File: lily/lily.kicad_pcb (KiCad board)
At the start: 4 copper layers, 70.7 x 53.3 mm, 23 parts, among them J1 NEIGHBOR1, J10 TEST_2P, J2 NEIGHBOR2, J3 ANT_IN, J4 TEST_2P, J5 TEST_2P, J6 TEST_2P, J7 BONUS_ROW, J8 TEST_2P, J9 TEST_2P, U1 ADL5904

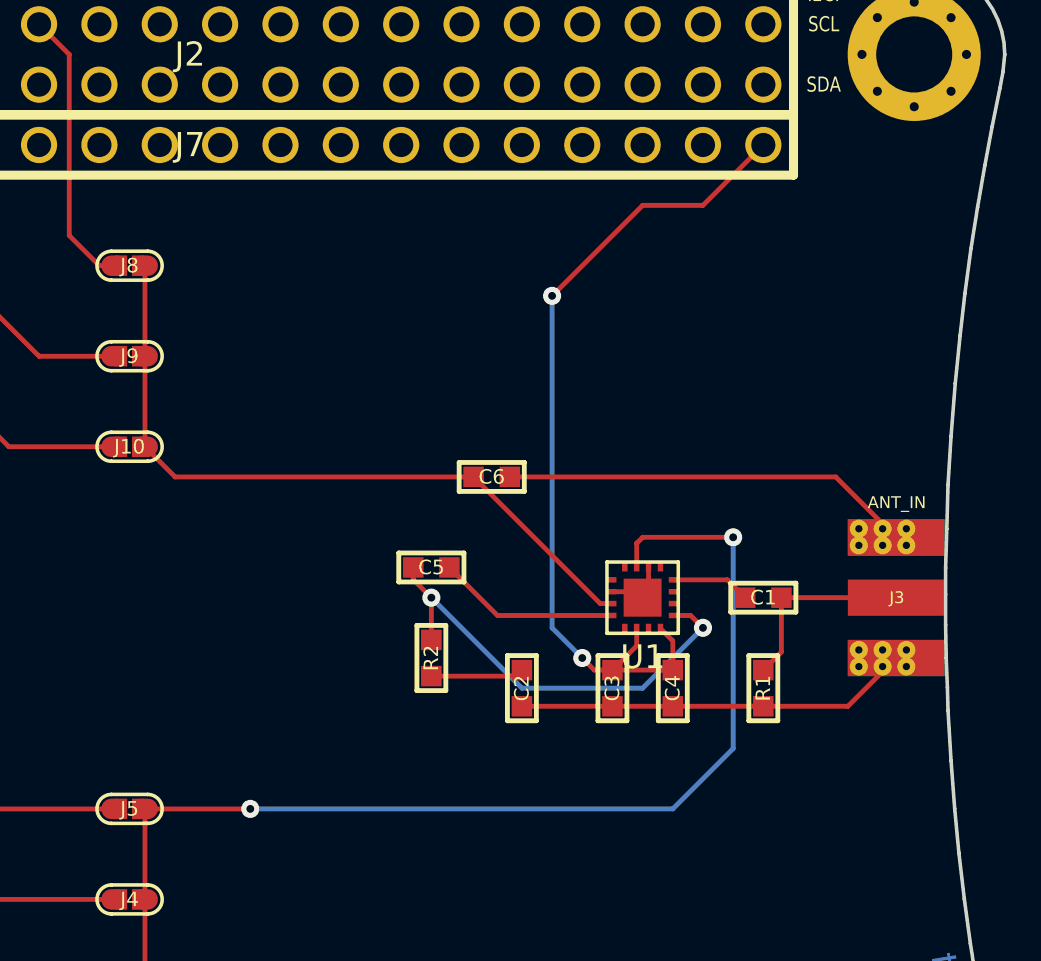
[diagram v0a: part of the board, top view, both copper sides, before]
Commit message: Updated copper pours on Lily PCB layout, added comments on schematic.
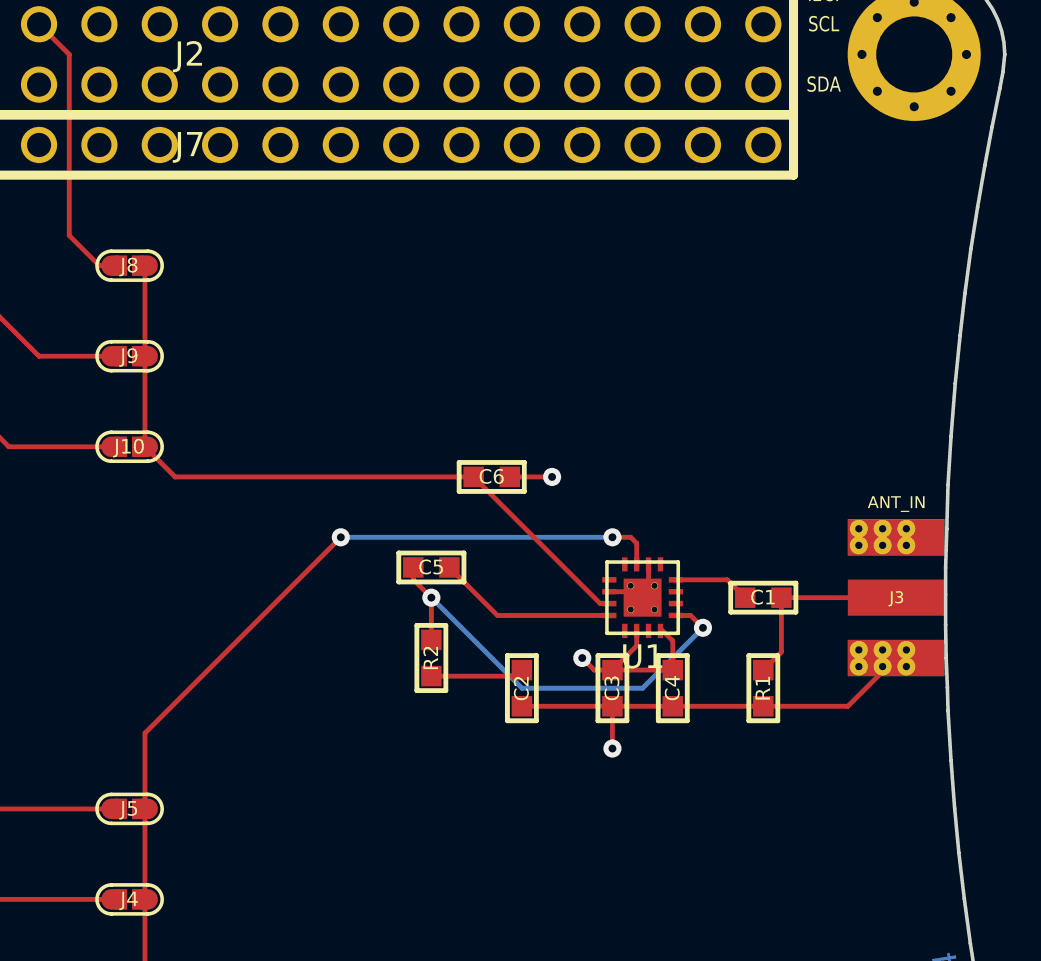
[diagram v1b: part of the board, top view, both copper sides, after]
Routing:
- net VCC: track 35.4 -> 8.15 mm, vias 2 -> 1
- net GND: track 36.7 -> 23.0 mm, vias 0 -> 2
- net /ENBL: track 47.5 -> 36.0 mm

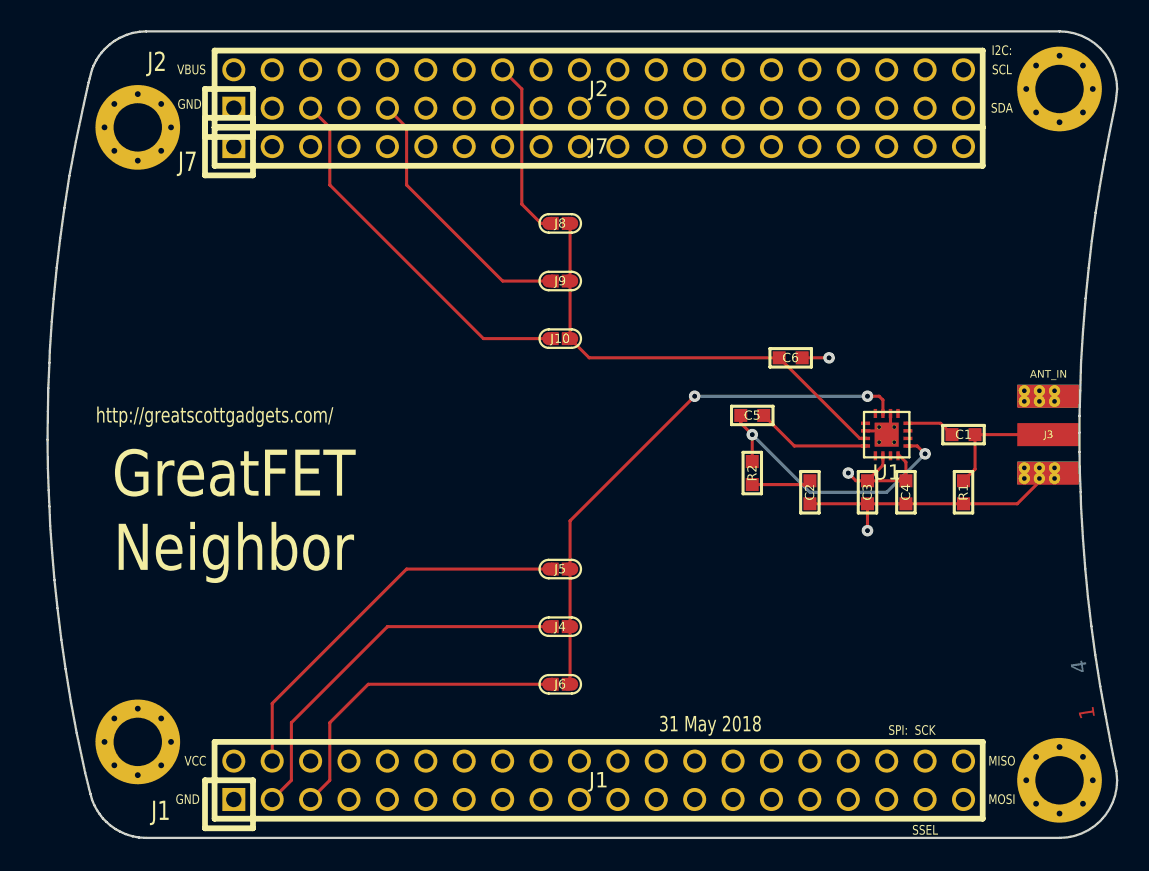
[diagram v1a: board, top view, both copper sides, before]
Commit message: Revised Lily schematic and PCB: Added connections for threshold detection mode and improved RF impedance matching.
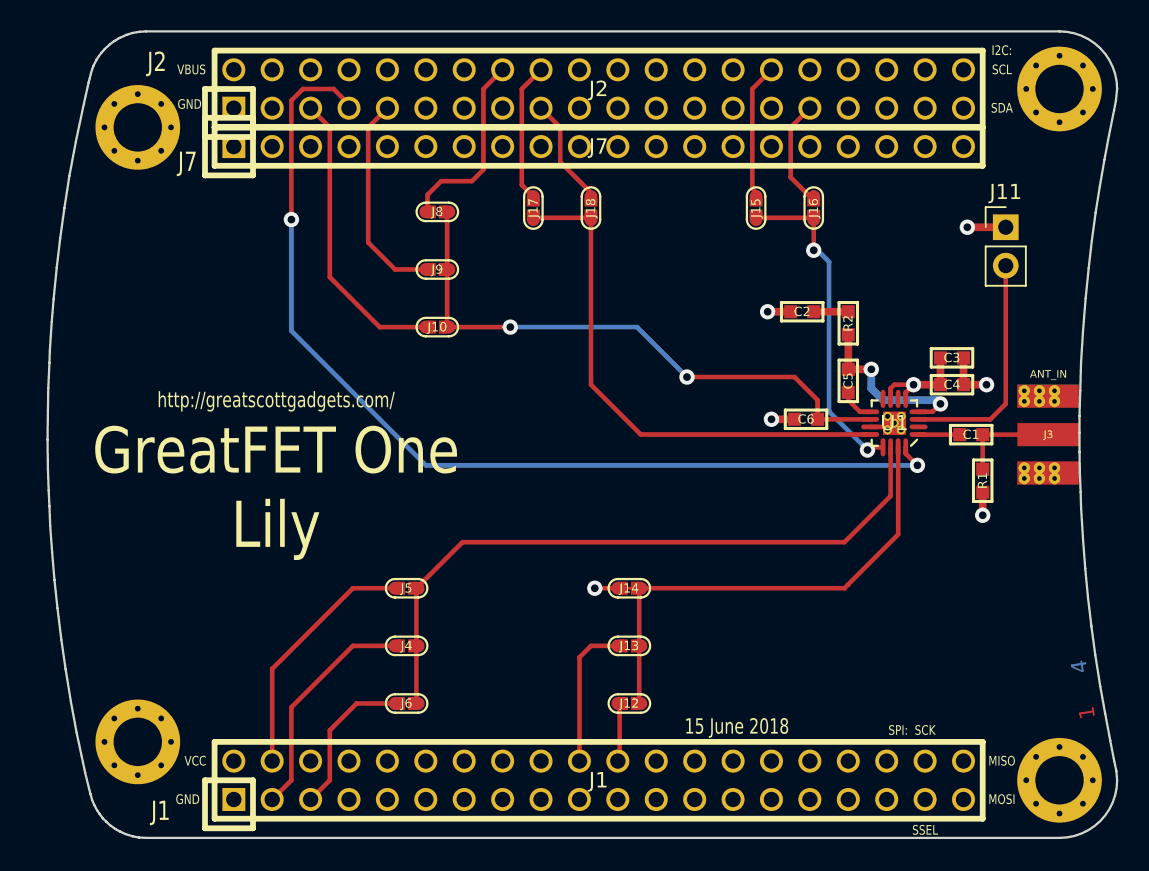
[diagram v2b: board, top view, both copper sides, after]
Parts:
- added J11: Conn_01x02, Pin_Headers:Pin_Header_Straight_1x02_Pitch2.54mm, F.Cu at (173.0, 81.5)
- added J12: TEST_2P, gsg-modules:0603-JUMPER, F.Cu at (148.1, 113.0)
- added J13: TEST_2P, gsg-modules:0603-JUMPER, F.Cu at (148.1, 109.2)
- added J14: TEST_2P, gsg-modules:0603-JUMPER, F.Cu at (148.1, 105.4)
- added J15: TEST_2P, gsg-modules:0603-JUMPER, F.Cu at (156.5, 80.3)
- added J16: TEST_2P, gsg-modules:0603-JUMPER, F.Cu at (160.3, 80.3)
- added J17: TEST_2P, gsg-modules:0603-JUMPER, F.Cu at (141.7, 80.3)
- added J18: TEST_2P, gsg-modules:0603-JUMPER, F.Cu at (145.5, 80.3)
- C3: value 0.1uF -> 100nF
- C5: value Crms -> 100nF
- U1: footprint gsg-modules:ADL5904 -> gsg-modules:QFN16-3
- moved C2 11.9 mm to (159.5, 87.1), turned to 180 degrees
- moved R2 11.8 mm to (162.6, 87.9), turned to 90 degrees
- moved C3 10.5 mm to (169.4, 90.2), turned to 0 degrees
- moved J4 10.2 mm to (133.3, 109.2)
- moved J5 10.2 mm to (133.3, 105.4)
- moved J6 10.2 mm to (133.3, 113.0)
- moved J10 8.16 mm to (135.4, 88.1)
- moved J8 8.16 mm to (135.4, 80.5)
- moved J9 8.16 mm to (135.4, 84.3)
- moved C4 7.74 mm to (169.4, 91.9), turned to 0 degrees
- moved C5 6.75 mm to (162.6, 91.7), turned to 90 degrees
- moved C6 4.19 mm to (159.8, 94.2), turned to 180 degrees
- moved R1 1.48 mm to (171.4, 98.3)
- moved U1 0.92 mm to (165.6, 94.5), turned to 180 degrees
- moved C1 0.51 mm to (170.7, 95.2)
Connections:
- net Net-(J2-Pad2) renamed /VBUS
- U1 pad 15: GND -> Net-(J12-Pad2)
- U1 pad 16: Net-(U1-Pad16) -> /P4_4
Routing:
- net /P4_4: track 0.00 -> 66.6 mm, vias 0 -> 2
- net Net-(J17-Pad1): track 0.00 -> 34.7 mm
- net Net-(J12-Pad2): track 0.00 -> 32.0 mm
- net Net-(J15-Pad1): track 0.00 -> 21.9 mm, vias 0 -> 2
- net Net-(J11-Pad2): track 0.00 -> 15.3 mm
- net /P4_10: track 21.3 -> 10.3 mm
- net /P4_9: track 25.4 -> 15.3 mm
- net /P1_10: track 0.00 -> 9.83 mm
- net /P2_5: track 0.00 -> 9.34 mm
- net /P3_7: track 0.00 -> 9.13 mm
- net /P0_0: track 25.9 -> 16.8 mm
- net /VOUT: track 30.0 -> 38.9 mm, vias 0 -> 2
- net /ENBL: track 36.0 -> 44.7 mm, vias 2 -> 0
- net GND: track 23.0 -> 14.8 mm, vias 2 -> 6
- net /WAKEUP0: track 0.00 -> 7.32 mm
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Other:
- board text added: "15 June 2018"
- board text added: "GreatFET One Lily"
- board text removed: "31 May 2018"
- board text removed: "GreatFET Neighbor"
- board text removed: "need to connect exposed pad to ground plane"

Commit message: Revised Lily PCB: added silkscreen labels, rerouted tracks, etc.
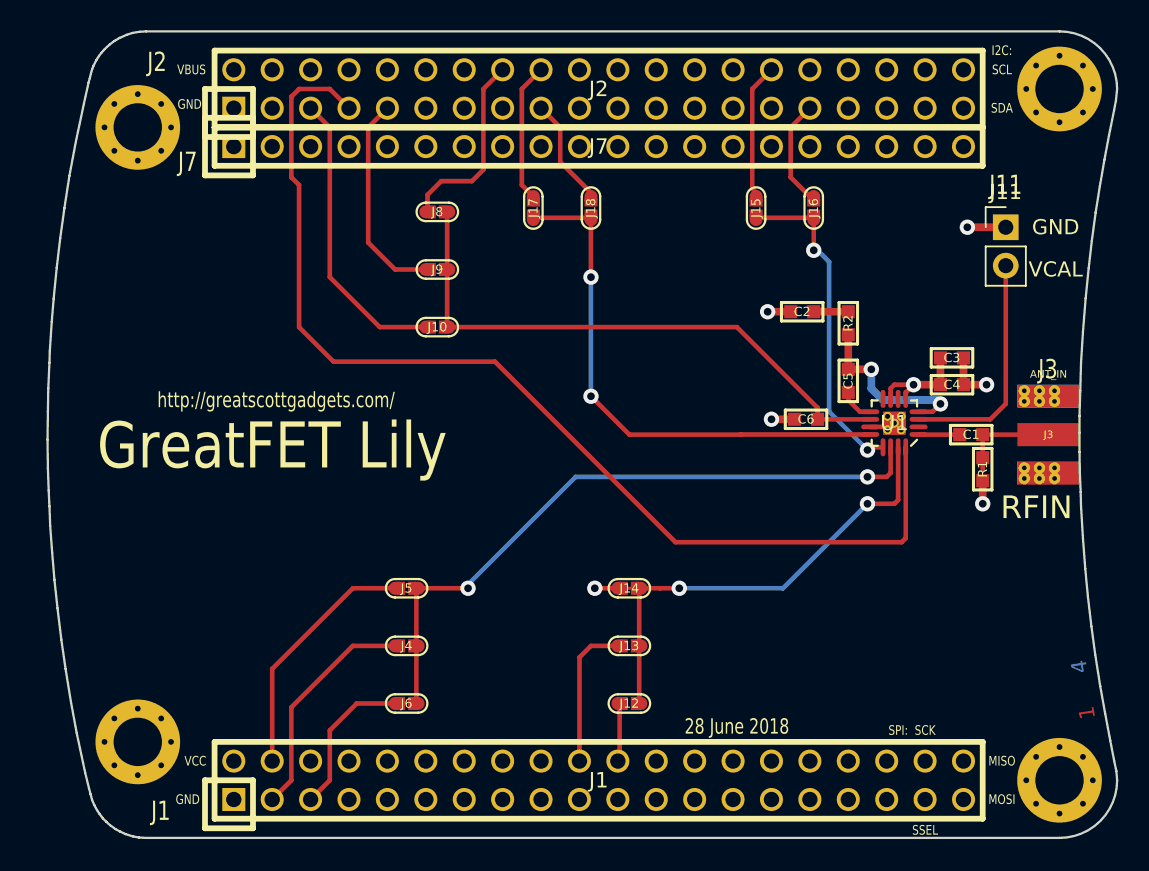
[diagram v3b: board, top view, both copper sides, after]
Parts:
- moved R1 0.76 mm to (171.4, 97.5)
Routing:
- net /P4_4: track 66.6 -> 72.8 mm, vias 2 -> 0
- net Net-(J12-Pad2): track 32.0 -> 30.7 mm, vias 0 -> 2
- net /ENBL: track 44.7 -> 44.0 mm, vias 0 -> 2
- net Net-(J17-Pad1): track 34.7 -> 35.1 mm, vias 0 -> 2
- net /VOUT: track 38.9 -> 38.6 mm, vias 2 -> 0
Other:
- board text added: "28 June 2018"
- board text added: "GreatFET Lily"
- board text added: "J11"
- board text added: "J3"
- board text added: "RFIN"
- board text added: "VCAL"
- board text removed: "15 June 2018"
- board text removed: "GreatFET One Lily"

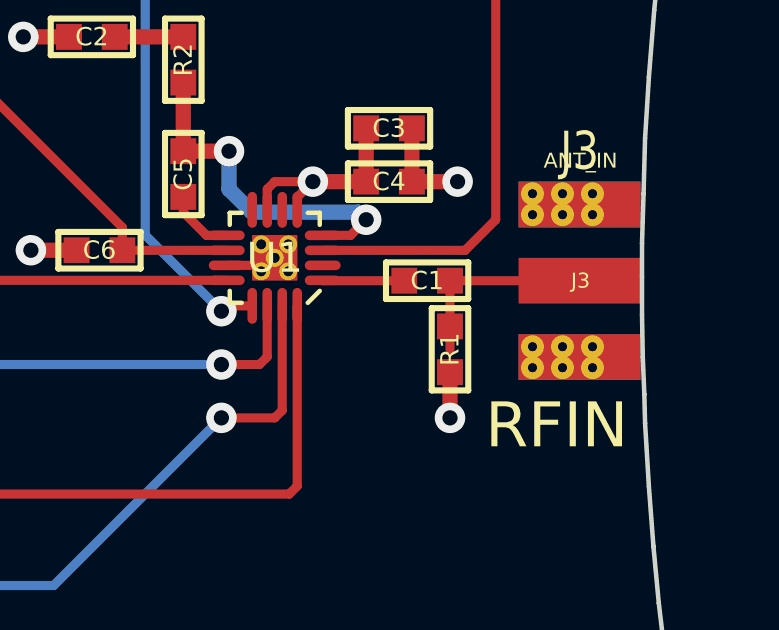
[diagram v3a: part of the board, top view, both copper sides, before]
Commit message: Fixed bad track
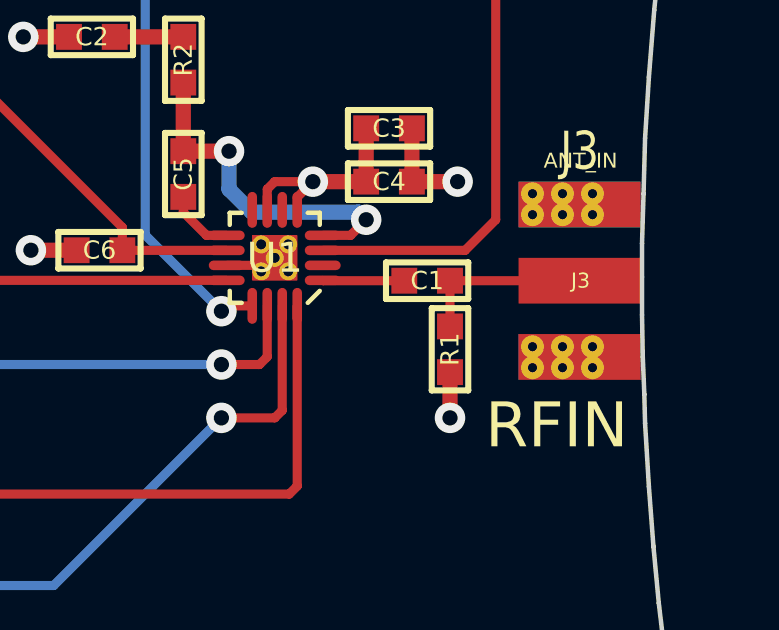
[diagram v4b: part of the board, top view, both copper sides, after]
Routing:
- net Net-(C1-Pad2): track 6.60 -> 5.84 mm
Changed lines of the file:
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@@
   (general
     (links 140)
-    (no_connects 3)
+    (no_connects 2)
     (area 107.95 66.04 279.525801 124.460001)
     (thickness 1.6)
@@
   (segment (start 164.008 94.238) (end 160.532 94.238) (width 0.3048) (layer F.Cu) (net 96))
   (segment (start 160.532 94.238) (end 160.528 94.234) (width 0.3048) (layer F.Cu) (net 96))
-  (segment (start 171.45 95.25) (end 171.45 97.536) (width 0.3048) (layer F.Cu) (net 97))
+  (segment (start 171.45 96.774) (end 171.45 95.25) (width 0.3048) (layer F.Cu) (net 97) (status C00000))
   (segment (start 171.45 95.25) (end 175.768 95.25) (width 0.3048) (layer F.Cu) (net 97))
   (segment (start 162.56 87.122) (end 160.274 87.122) (width 0.508) (layer F.Cu) (net 98))
